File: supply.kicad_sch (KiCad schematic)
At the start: 96 parts, among them J11 205338-0002, J4 282834-2, Q1 BSS138DWQ-7, Q10 MBT2222ADW1T1, Q5 PJE138K, Q6 SSM3J332R, Q7 MBT2222ADW1T1, Q8 PJE138K, Q9 BSS138DWQ-7, SW1 SW_SPDT, U1 TPS56C230, U29 TPS56C230, U41 NCP730BMT330, U42 TPS7A0518P, U6 ADM1176-1ARMZ-R7

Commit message: Initial layout attempt
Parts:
- removed J11: 205338-0002, JetsonCarrier:MOLEX_2053380002, symbol Connector_Generic_MountingPin:Conn_01x02_MountingPin
- removed J4: 282834-2, JetsonCarrier:TE_282834-2, symbol Connector_Generic:Conn_01x02
- added J6: 205338-0004, Connector_Molex:Molex_Pico-Lock_205338-0004_1x04-1MP_P2.00mm_Horizontal, symbol Connector_Generic_MountingPin:Conn_01x04_MountingPin
- added J8: 282834-4, Argus-Connectors:TE_282834-4, symbol Connector_Generic:Conn_01x04
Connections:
- net GND: now also J6.3 (Pin_3), J6.4 (Pin_4), J6.MP (MountPin), J8.3 (Pin_3), J8.4 (Pin_4)
- net VBATT: now also J6.1 (Pin_1), J6.2 (Pin_2), J8.1 (Pin_1), J8.2 (Pin_2)
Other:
- note added: "Add full poweroff sequencing"
- moved on the sheet: D7

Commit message: Add power sequencing logic, layout
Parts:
- removed C28, C30: 10nF, Capacitor_SMD:C_0603_1608Metric, symbol Device:C_Small
- removed Q1, Q9: BSS138DWQ-7, Package_TO_SOT_SMD:SOT-363_SC-70-6, symbol JetsonCarrier:BSS138DWQ-7
- removed Q10, Q7: MBT2222ADW1T1, Package_TO_SOT_SMD:SOT-363_SC-70-6, symbol Transistor_BJT:MBT2222ADW1T1
- removed R59, R75: 680R, Resistor_SMD:R_0603_1608Metric, symbol Device:R_Small
- removed R65, R76: 100k, Resistor_SMD:R_0603_1608Metric, symbol Device:R_Small
- removed R68, R69, R77, R78: 10k, Resistor_SMD:R_0603_1608Metric, symbol Device:R_Small
- removed R70, R79: 200k, Resistor_SMD:R_0603_1608Metric, symbol Device:R_Small
- removed R71, R74: 0R, Resistor_SMD:R_0603_1608Metric, symbol Device:R_Small
- added C10, C7, C8, C9: 100nF, Capacitor_SMD:C_0603_1608Metric, symbol Device:C_Small
- added C109: 1uF, Capacitor_SMD:C_0603_1608Metric, symbol Device:C_Small
- added R115, R116, R193, R194: 10k, Resistor_SMD:R_0603_1608Metric, symbol Device:R_Small
- added R191, R192: 0R, Resistor_SMD:R_0603_1608Metric, symbol Device:R_Small
- added U12: SN74AHC1G32, Package_TO_SOT_SMD:SOT-353_SC-70-5, symbol 74xGxx:74AHC1G32
- added U13: SN74LVC1G11, Package_TO_SOT_SMD:SOT-363_SC-70-6, symbol 74xGxx:74LVC1G11
- added U14: SN74LVC1G175, Package_TO_SOT_SMD:SOT-363_SC-70-6, symbol 74xGxx:74LVC1G175
- added U15: 74LVC1G17, Package_TO_SOT_SMD:SOT-353_SC-70-5, symbol 74xGxx:74LVC1G17
- R155: footprint Resistor_SMD:R_0402_1005Metric -> Resistor_SMD:R_0603_1608Metric
- R161, R162, R82: now not fitted; now left out of the parts list
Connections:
- net JETSON_EN is gone; now on an unnamed net: SW1.1
- net 3V3_STDB: now also BTN3.2, C10.1, C7.1, C8.1, C9.1, R116.2, R192.1, R193.1, U12.5 (VCC), U13.5 (VCC), U14.5 (VCC), U15.5 (VCC); no longer BTN3.1
- net 5V0_EN: now also U12.4
- net GND: now also C10.2, C109.2, C7.2, C8.2, C9.2, R115.1, U12.3 (GND), U13.2 (GND), U14.2 (GND), U15.3 (GND)
- net POWER_EN: now also R191.2; no longer R155.2
- net ~{RESET}: now also U12.2
- net REG_PG: now reaches R162.2, U29.9 (PG)
- net REG_PG: now also R161.2, U1.9 (PG), R193.2, R194.1
- net at C103.2, D16.2 (A2), Q8.1 (G)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: now also BTN3.1; no longer BTN3.2
- net at R14.1: no longer SW1.3
- net PWR_SCL renamed I2C Protection/SCL_DEVICE
- net PWR_SDA renamed I2C Protection/SDA_DEVICE
- new net: C109.1, R194.2, U15.2
- new net: R192.2, U14.3 (D)
- new net: R191.1, U14.4 (Q)
- new net: U13.4, U14.6 (~{CLR})
- new net 5V0_PG_DELAYED: U14.1 (C), U15.4
- new net MASTER_EN: R155.2, U12.1, U13.3
- new net MB_MASTER_EN: R115.2, SW1.3
- new net ~{MB_SHUTDOWN_REQ}: R116.1, U13.1
- new net ~{SHUTDOWN_REQ}: U13.6
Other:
- added sheet I2C Protection (I2C_Protection.kicad_sch)
- note added: "POWER SELECTOR SWITCH"
- note removed: "Add full poweroff sequencing"
- note removed: "I2C Bus Protection - Power Monitor & USB Charger"
- note removed: "TODO: USE 3V3_STDB instead?"
- moved on the sheet: BTN3, C103, C26, C5, C58, C59, C6, C65, C76, C77, C93, D14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

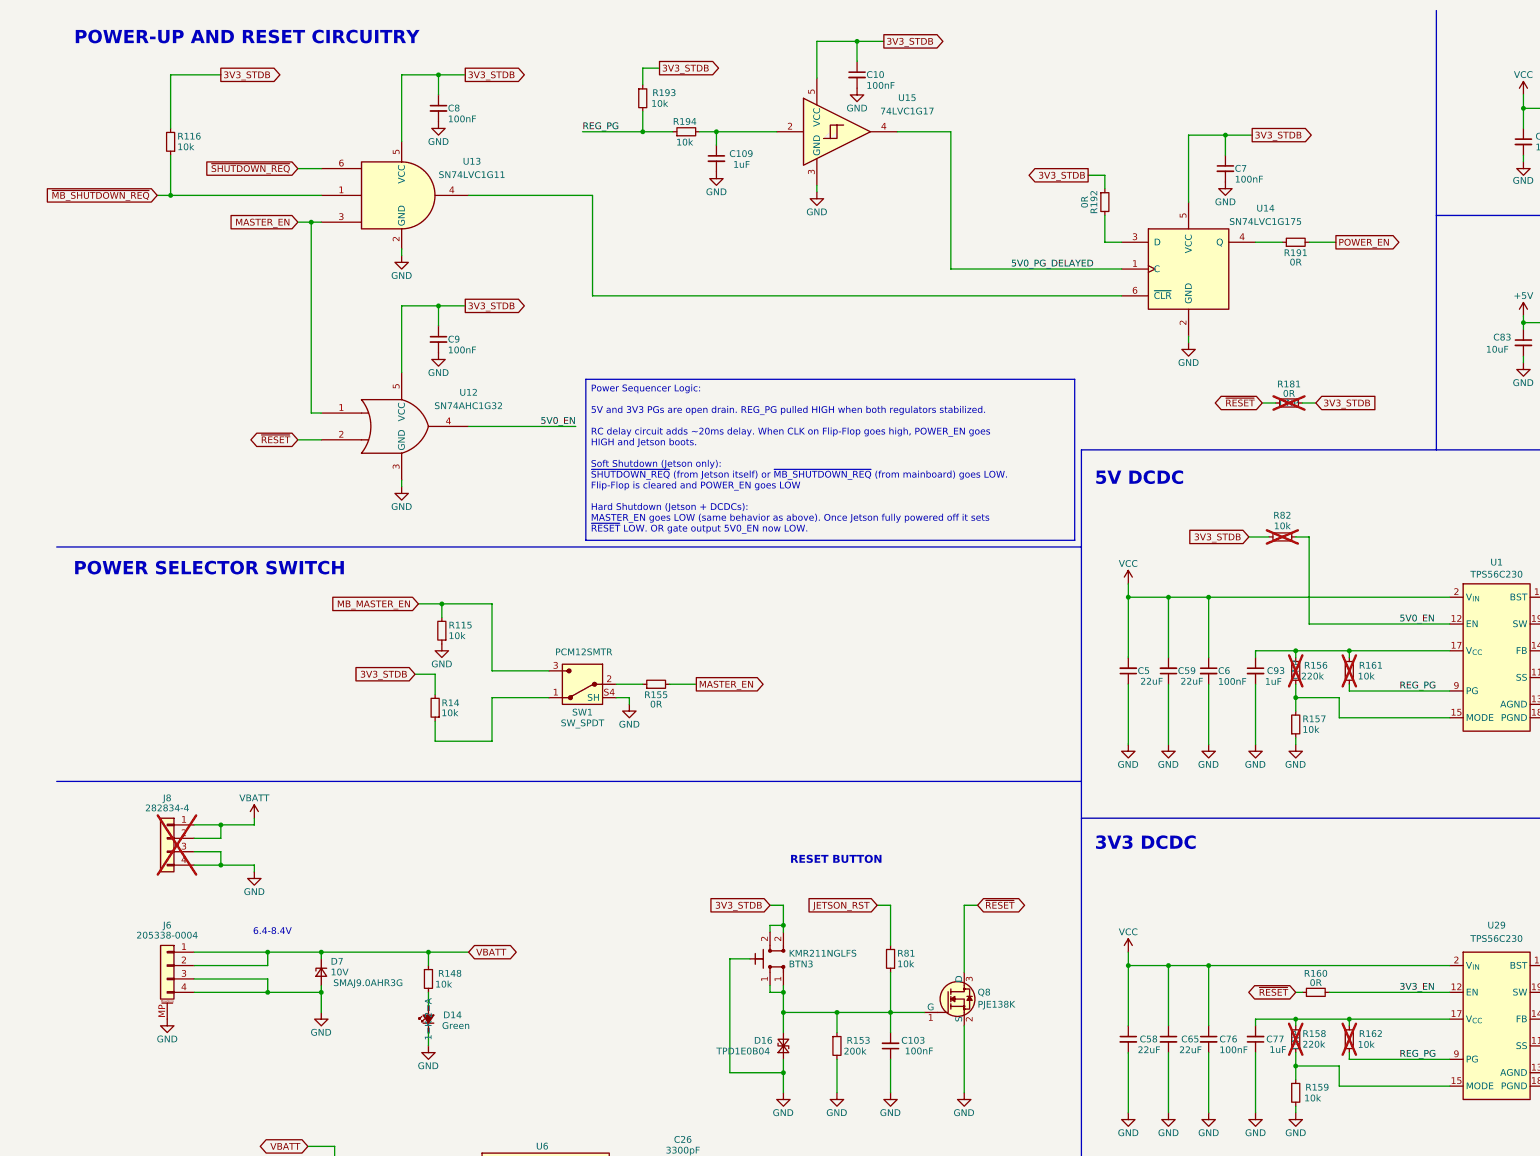
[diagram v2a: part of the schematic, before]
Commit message: Add bus protection, upgrade sequencer
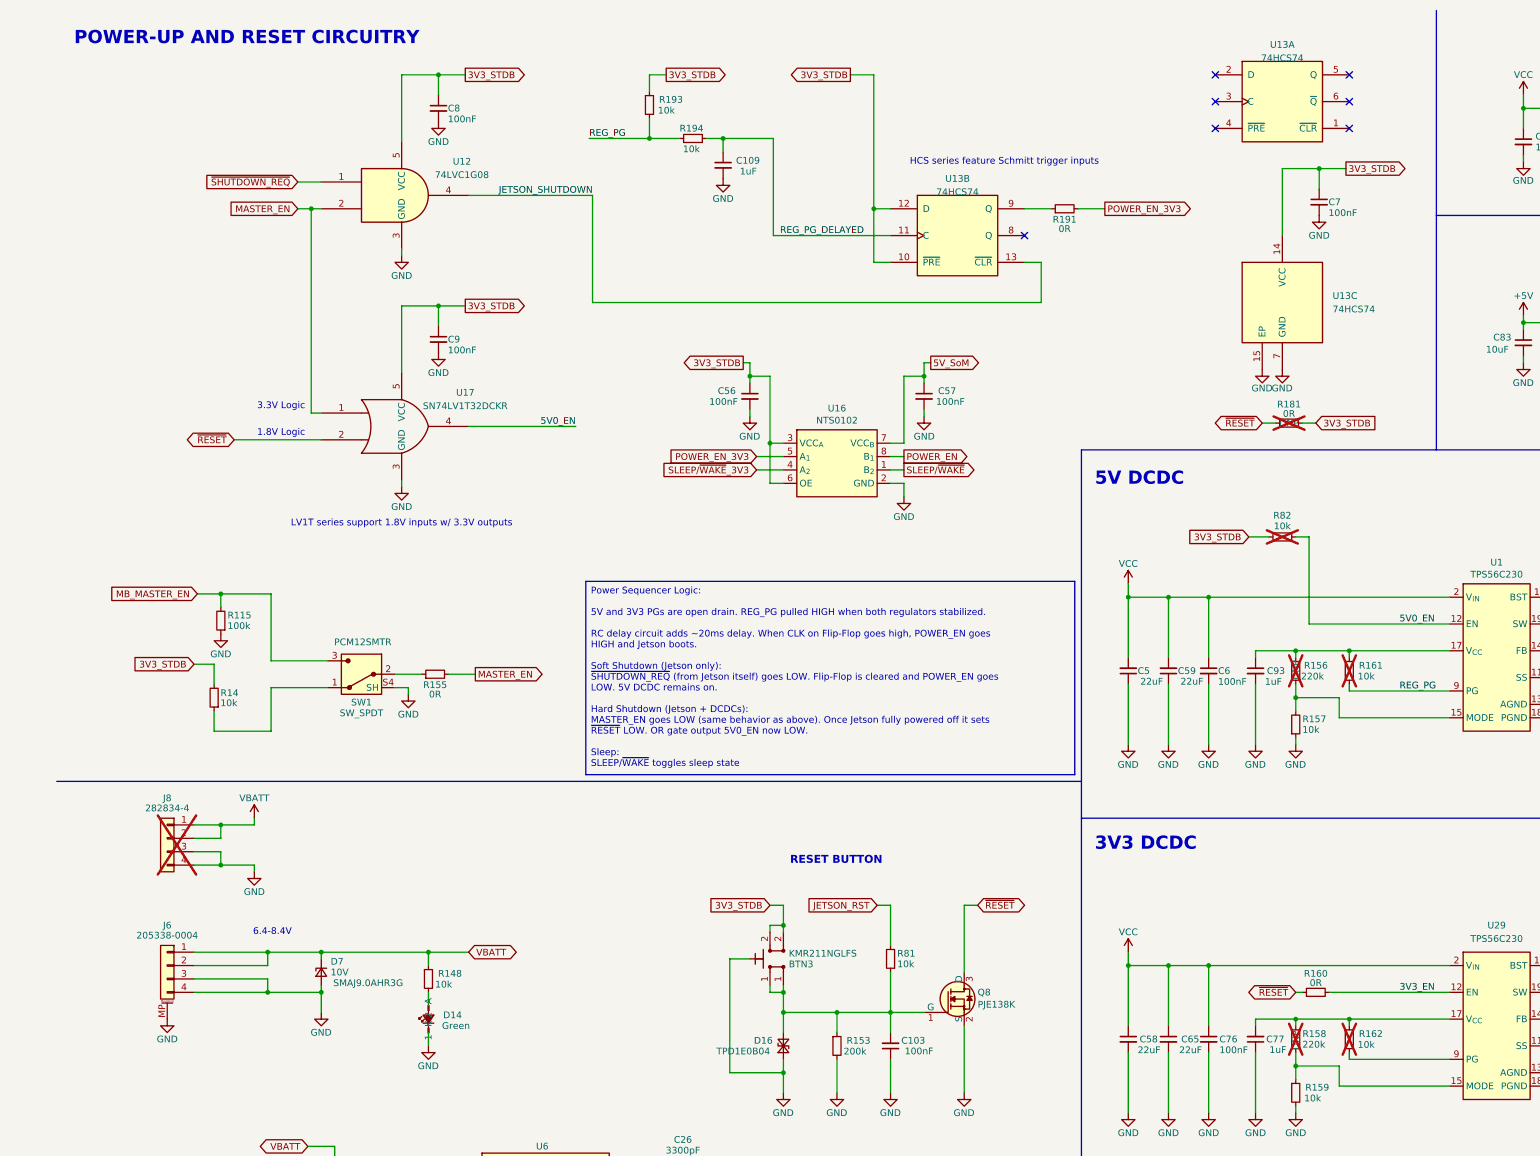
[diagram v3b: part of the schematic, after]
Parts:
- removed C10: 100nF, Capacitor_SMD:C_0603_1608Metric, symbol Device:C_Small
- removed R116: 10k, Resistor_SMD:R_0603_1608Metric, symbol Device:R_Small
- removed R192: 0R, Resistor_SMD:R_0603_1608Metric, symbol Device:R_Small
- removed U12: SN74AHC1G32, Package_TO_SOT_SMD:SOT-353_SC-70-5, symbol 74xGxx:74AHC1G32
- removed U13: SN74LVC1G11, Package_TO_SOT_SMD:SOT-363_SC-70-6, symbol 74xGxx:74LVC1G11
- removed U14: SN74LVC1G175, Package_TO_SOT_SMD:SOT-363_SC-70-6, symbol 74xGxx:74LVC1G175
- removed U15: 74LVC1G17, Package_TO_SOT_SMD:SOT-353_SC-70-5, symbol 74xGxx:74LVC1G17
- added C56, C57: 100nF, Capacitor_SMD:C_0603_1608Metric, symbol Device:C_Small
- added U12: 74LVC1G08, Package_TO_SOT_SMD:SOT-353_SC-70-5, symbol 74xGxx:74LVC1G08
- added U13: 74HCS74, Package_DFN_QFN:DHWQFN-14-1EP_2.5x3mm_P0.5mm_EP1x1.5mm_ThermalVias, symbol Argus-IC:74HCS74
- added U16: NTS0102, Argus-IC:NXP_XSON-8, symbol JetsonCarrier:NTS0102
- added U17: SN74LV1T32DCKR, Package_TO_SOT_SMD:SOT-353_SC-70-5, symbol 74xGxx:74LVC1G32
- R115: value 10k -> 100k
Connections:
- net 3V3_STDB: now also C56.1, U12.5 (VCC), U13.10 (~{PRE}), U13.12 (D), U13.14 (VCC), U16.3 (VCC_{A}), U16.6 (OE), U17.5 (VCC)
- net 5V0_EN: now also U17.4
- net 5V_SoM: now also C57.1, U16.7 (VCC_{B})
- net GND: now also C56.2, C57.2, U12.3 (GND), U13.15 (EP), U13.7 (GND), U16.2 (GND), U17.3 (GND)
- net MASTER_EN: now also U12.2, U17.1
- net POWER_EN: now also U16.8 (B_{1}); no longer R191.2
- net REG_PG: no longer R162.2, U29.9 (PG)
- net ~{RESET}: now also U17.2
- net ~{SHUTDOWN_REQ}: now also U12.1
- net REG_PG_DELAYED: now reaches C109.1, R194.2
- net REG_PG_DELAYED: now also U13.11 (C)
- net at R191.1: now also U13.9 (Q)
- new net: R162.2, U29.9 (PG)
- new net JETSON_SHUTDOWN: U12.4, U13.13 (~{CLR})
- new net POWER_EN_3V3: R191.2, U16.5 (A_{1})
- new net SLEEP/~{WAKE}: U16.1 (B_{2})
- new net SLEEP/~{WAKE}_3V3: U16.4 (A_{2})
- no-connect marks 3 -> 10
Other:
- note added: "1.8V Logic"
- note added: "3.3V Logic"
- note added: "HCS series feature Schmitt trigger inputs"
- note added: "LV1T series support 1.8V inputs w/ 3.3V outputs"
- note removed: "POWER SELECTOR SWITCH"
- moved on the sheet: C109, C7, R115, R14, R155, R181, R191, R193, R194, SW1

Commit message: Layout cleanup, silk
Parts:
- TP21, TP23, TP24, TP28: footprint JetsonCarrier:TP_SMD_0.75mm -> TestPoint:TestPoint_Pad_D1.0mm
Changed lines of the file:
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@@
 			)
 		)
-		(property "Footprint" "JetsonCarrier:TP_SMD_0.75mm"
+		(property "Footprint" "TestPoint:TestPoint_Pad_D1.0mm"
 			(at 378.46 76.2 0)
 			(hide yes)
@@
 			)
 		)
-		(property "Footprint" "JetsonCarrier:TP_SMD_0.75mm"
+		(property "Footprint" "TestPoint:TestPoint_Pad_D1.0mm"
 			(at 359.41 29.21 0)
 			(hide yes)
@@
 			)
 		)
-		(property "Footprint" "JetsonCarrier:TP_SMD_0.75mm"
+		(property "Footprint" "TestPoint:TestPoint_Pad_D1.0mm"
 			(at 398.78 120.65 0)
 			(hide yes)
@@
 			)
 		)
-		(property "Footprint" "JetsonCarrier:TP_SMD_0.75mm"
+		(property "Footprint" "TestPoint:TestPoint_Pad_D1.0mm"
 			(at 377.19 203.2 0)
 			(hide yes)
